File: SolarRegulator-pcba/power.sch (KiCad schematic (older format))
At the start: 59 parts

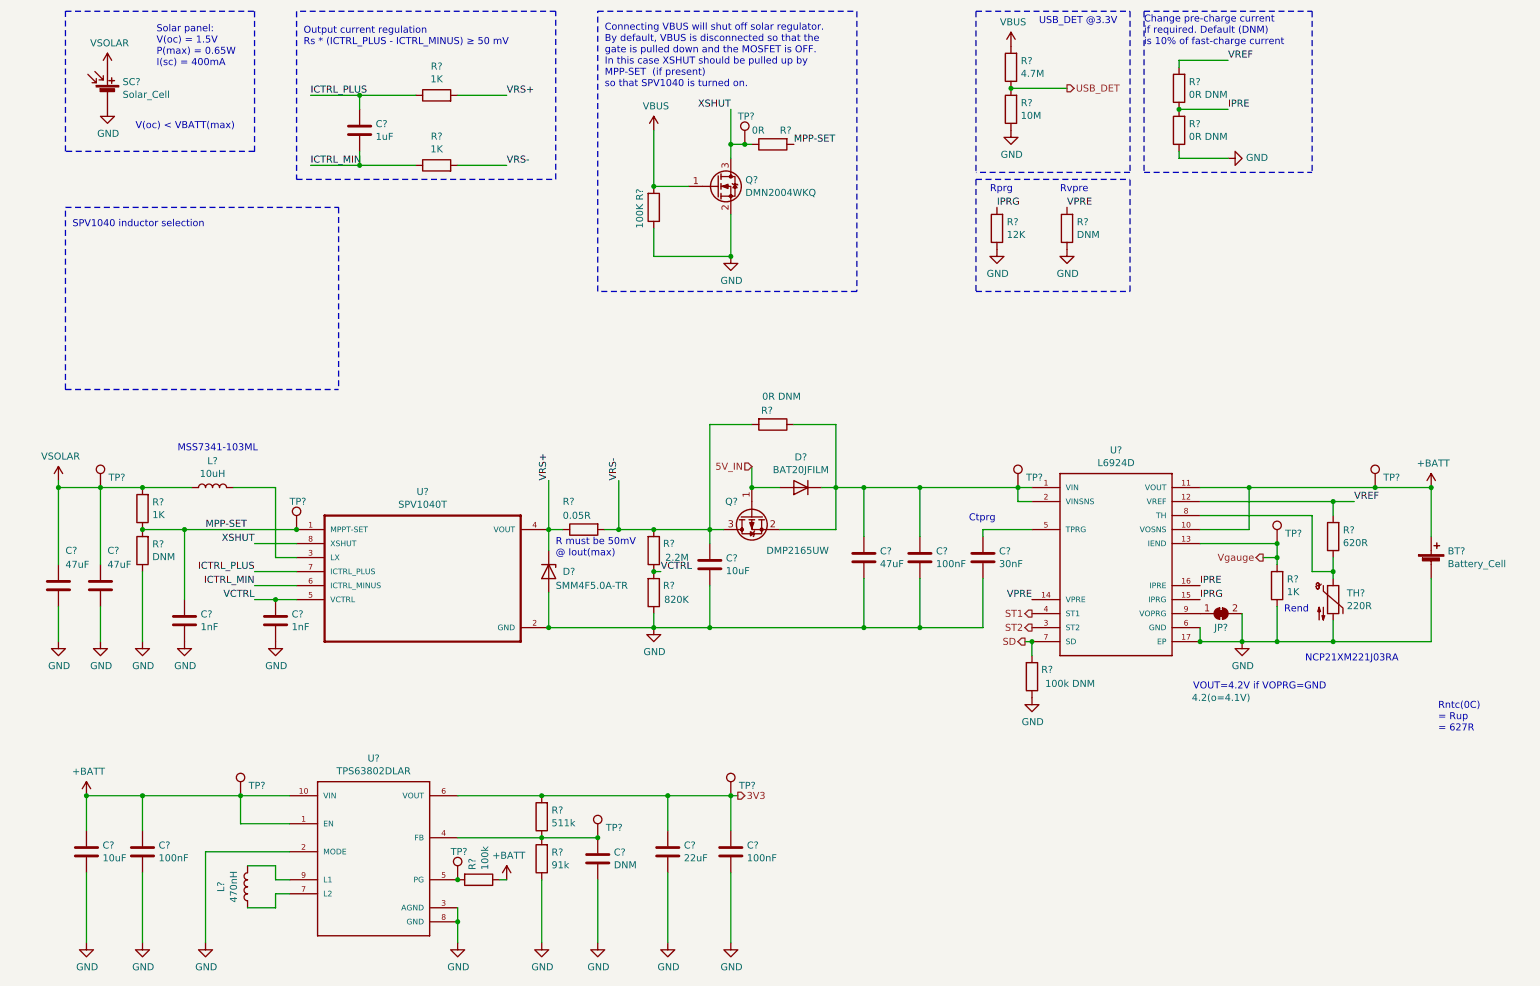
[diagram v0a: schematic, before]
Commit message: Add more footprints to schematic and pcb
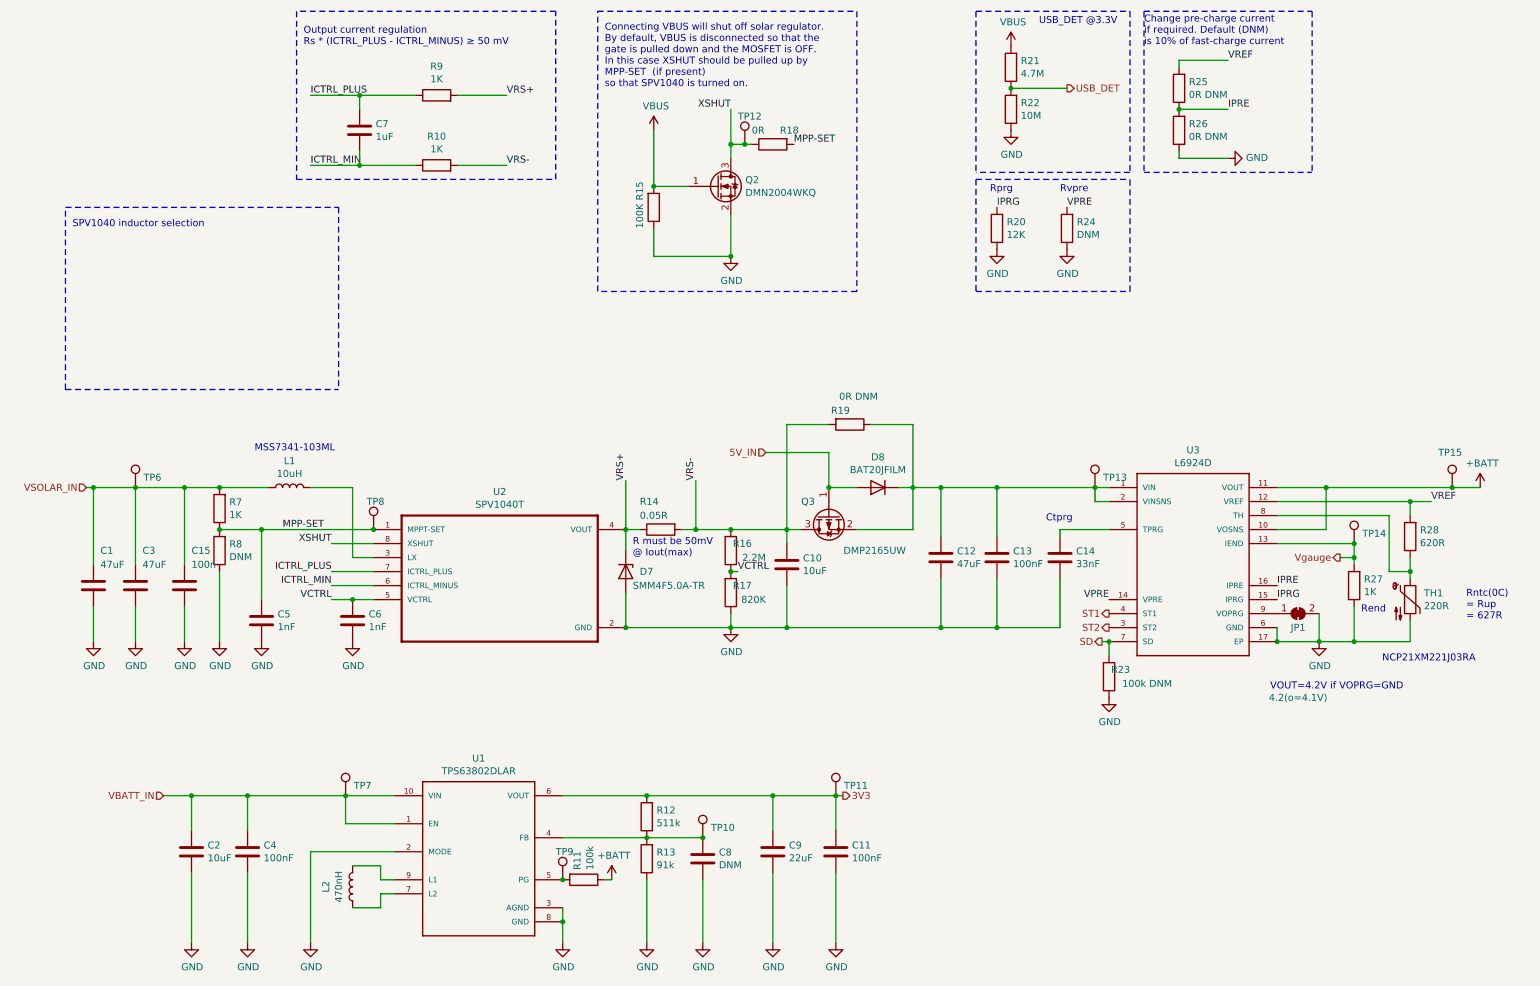
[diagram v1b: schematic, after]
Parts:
- removed BT?: Battery_Cell, Connector_JST:JST_PH_S2B-PH-SM4-TB_1x02-1MP_P2.00mm_Horizontal, symbol Device:Battery_Cell
- removed SC?: Solar_Cell, Connector_JST:JST_PH_S2B-PH-SM4-TB_1x02-1MP_P2.00mm_Horizontal, symbol Device:Solar_Cell
- added C15: 100n, symbol Device:C
- C1, C12, C3: renamed from C?; footprint (none) -> Capacitor_SMD:C_1206_3216Metric_Pad1.42x1.75mm_HandSolder
- C10, C11, C13, C2, C4, C5, C6, C8, C9: renamed from C?; footprint (none) -> Capacitor_SMD:C_0805_2012Metric_Pad1.15x1.40mm_HandSolder
- C14: renamed from C?; value 30nF -> 33nF; footprint (none) -> Capacitor_SMD:C_0805_2012Metric_Pad1.15x1.40mm_HandSolder
- Q2: renamed from Q?; footprint Package_TO_SOT_SMD:SOT-323_SC-70 -> Package_TO_SOT_SMD:SOT-323_SC-70_Handsoldering
- Q3: renamed from Q?; footprint (none) -> Package_TO_SOT_SMD:SOT-323_SC-70_Handsoldering
- TP10, TP11, TP12, TP13, TP14, TP15, TP6, TP7, TP8, TP9: renamed from TP?; footprint (none) -> TestPoint:TestPoint_Pad_D1.0mm
- U1: renamed from U?; footprint VREG_TPS63802DLAR -> TPS63802DLAR:VREG_TPS63802DLAR
- U2: renamed from U?; footprint SOP65P640X120-8N -> SPV1040T:SPV1040T
- U3: renamed from U?; footprint QFN50P300X300X100-17N -> L6924D:L6924D
- gave numbers to parts that had none: 29
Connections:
- net +BATT: no longer C2.1, C4.1, TP7.1, U1.1 (EN), U1.10 (VIN)
- net GND: now also C15.2
- net +1V0 renamed VSOLAR_IN
- net VSOLAR_IN: now also C15.1
- new net VBATT_IN: C2.1, C4.1, TP7.1, U1.1 (EN), U1.10 (VIN)
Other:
- note removed: "Solar panel:\nV(oc) = 1.5V\nP(max) = 0.65W\nI(sc) = 400mA"
- note removed: "V(oc) < VBATT(max)"
- moved on the sheet: C1, C10, C11, C12, C13, C14, C2, C3, C4, C5, C6, C8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

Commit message: Modify power.sch
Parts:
- L1: footprint (none) -> MSS7341-103ML:MSS7341-103ML
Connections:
- net VBATT_IN is gone; now on net +BATT: C2.1, C4.1, TP7.1, U1.1 (EN), U1.10 (VIN)
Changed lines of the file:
@@
 U 1 1 5F247ABB
 P 5550 4400
-F 0 "R16" H 5700 4350 50  0000 R CNN
+F 0 "R16" H 5800 4350 50  0000 R CNN
 F 1 "2.2M" H 5800 4450 50  0000 R CNN
 F 2 "Resistor_SMD:R_1206_3216Metric_Pad1.42x1.75mm_HandSolder" V 5480 4400 50  0001 C CNN
@@
 F 0 "L1" V 2590 3950 50  0000 C CNN
 F 1 "10uH" V 2499 3950 50  0000 C CNN
-F 2 "" H 2400 3950 50  0001 C CNN
+F 2 "MSS7341-103ML:MSS7341-103ML" H 2400 3950 50  0001 C CNN
 F 3 "~" H 2400 3950 50  0001 C CNN
 	1    2400 3950
@@
 $EndComp
 Connection ~ 6250 3950
-Text HLabel 5800 3700 0    50   Input ~ 0
+Text HLabel 5850 3950 0    50   Input ~ 0
 5V_IN
 Text HLabel 950  3950 0    50   Input ~ 0
@@
 Connection ~ 1900 3950
 Wire Wire Line
-	5800 3700 6250 3700
-Wire Wire Line
-	6250 3700 6250 3950
+	5850 3950 6250 3950
+$Comp
+L power:+BATT #PWR0142
+U 1 1 5F3FBB4C
+P 1700 6150
+F 0 "#PWR0142" H 1700 6000 50  0001 C CNN
+F 1 "+BATT" H 1715 6323 50  0000 C CNN
+F 2 "" H 1700 6150 50  0001 C CNN
+F 3 "" H 1700 6150 50  0001 C CNN
+	1    1700 6150
+	1    0    0    -1
+$EndComp
 $EndSCHEMATC

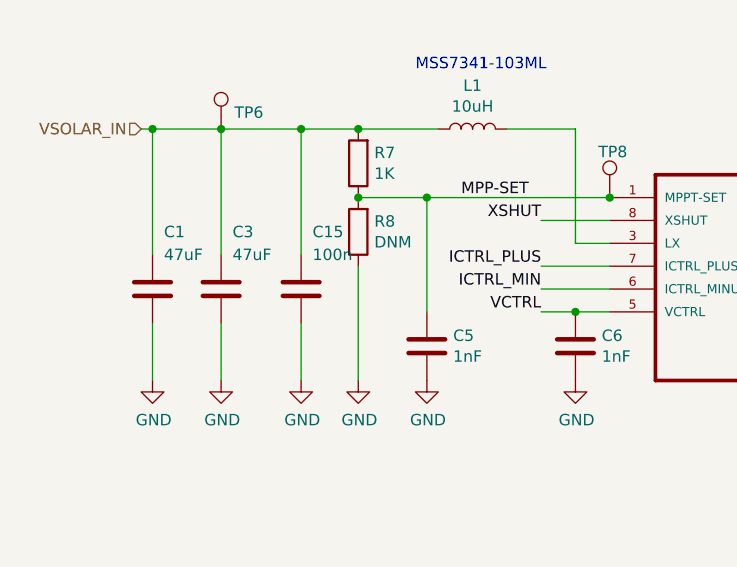
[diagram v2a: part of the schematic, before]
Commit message: Add final footprints, update LED footprints to 1206
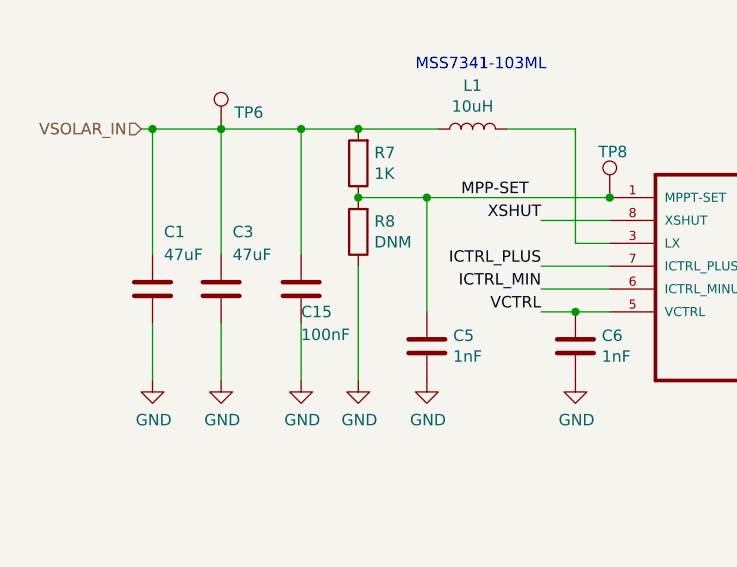
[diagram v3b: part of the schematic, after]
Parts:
- C15: value 100n -> 100nF; footprint (none) -> Capacitor_SMD:C_0805_2012Metric_Pad1.15x1.40mm_HandSolder
- C7: footprint (none) -> Capacitor_SMD:C_1206_3216Metric_Pad1.42x1.75mm_HandSolder
- D7: footprint (none) -> SMM4FxxA:SMM4FxxA
- JP1: footprint (none) -> Jumper:SolderJumper-2_P1.3mm_Bridged_RoundedPad1.0x1.5mm
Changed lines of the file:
@@
 F 0 "JP1" H 9600 4750 50  0000 C CNN
 F 1 "4.2(o=4.1V)" H 9600 4250 50  0000 C CNN
-F 2 "" H 9600 4850 50  0001 C CNN
+F 2 "Jumper:SolderJumper-2_P1.3mm_Bridged_RoundedPad1.0x1.5mm" H 9600 4850 50  0001 C CNN
 F 3 "~" H 9600 4850 50  0001 C CNN
 	1    9600 4850
@@
 F 0 "C7" H 3015 1446 50  0000 L CNN
 F 1 "1uF" H 3015 1355 50  0000 L CNN
-F 2 "" H 2938 1250 50  0001 C CNN
+F 2 "Capacitor_SMD:C_1206_3216Metric_Pad1.42x1.75mm_HandSolder" H 2938 1250 50  0001 C CNN
 F 3 "~" H 2900 1400 50  0001 C CNN
 	1    2900 1400
@@
 F 0 "D7" V 4800 4650 50  0000 L CNN
 F 1 "SMM4F5.0A-TR" V 4900 4600 50  0000 L CNN
-F 2 "" H 4800 4550 50  0001 C CNN
+F 2 "SMM4FxxA:SMM4FxxA" H 4800 4550 50  0001 C CNN
 F 3 "~" H 4800 4550 50  0001 C CNN
 	1    4800 4550
@@
 U 1 1 5F612BDC
 P 1650 4650
-F 0 "C15" H 1700 4900 50  0000 L CNN
-F 1 "100n" H 1700 4800 50  0000 L CNN
-F 2 "" H 1688 4500 50  0001 C CNN
+F 0 "C15" H 1650 4550 50  0000 L CNN
+F 1 "100nF" H 1650 4450 50  0000 L CNN
+F 2 "Capacitor_SMD:C_0805_2012Metric_Pad1.15x1.40mm_HandSolder" H 1688 4500 50  0001 C CNN
 F 3 "~" H 1650 4650 50  0001 C CNN
 	1    1650 4650
